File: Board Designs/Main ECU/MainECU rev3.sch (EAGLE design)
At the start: 155 parts, among them Q1 MMBT3904LT3G, Q11 MMBT3904LT3G, Q2 MMBT3904LT3G, Q3 MMBT3904LT3G, Q4 MMBT3904LT3G, Q5 MMBT3904LT3G, Q6 MMBT3904LT3G, Q7 MMBT3904LT3G, Q8 MMBT3904LT3G, Q9 MMBT3904LT3G, X1 CONNECTOR-37, X2 CONNECTOR-4AUTOSPORT, X3 CONNECTOR-4NANO-FIT-VERTICAL-4, X4 CONNECTOR-4NANO-FIT-VERTICAL-4

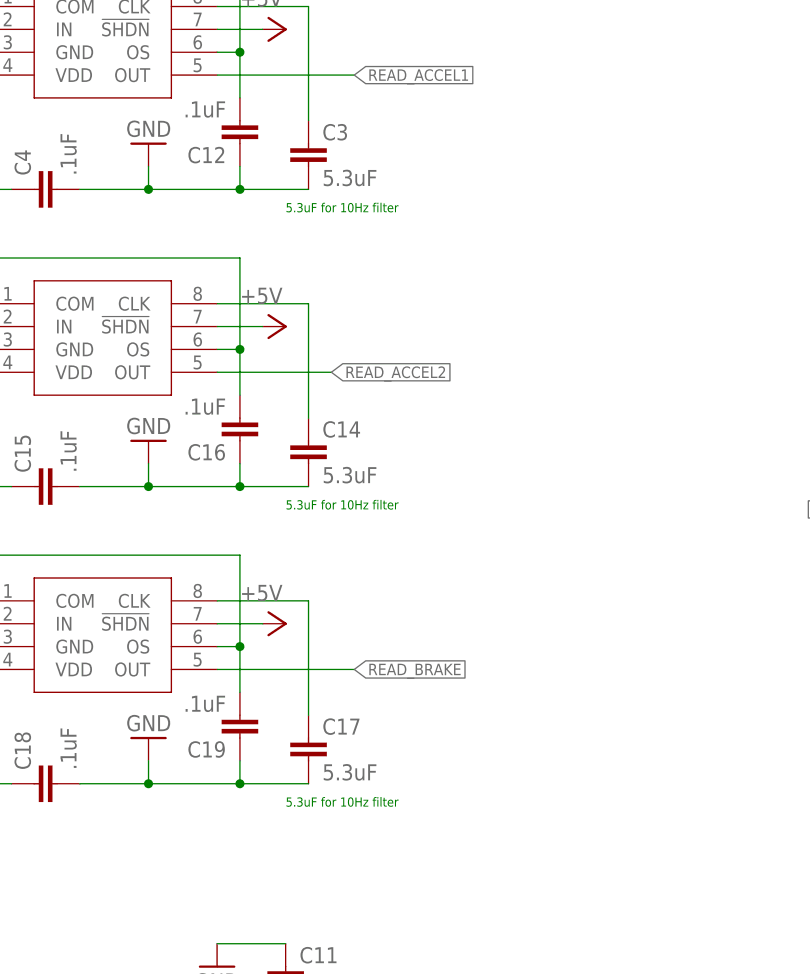
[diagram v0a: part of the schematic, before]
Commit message: Main ECU: [rev2, rev3] Fix filter frequency capacitor values, [rev1b, rev3] shorten a few traces
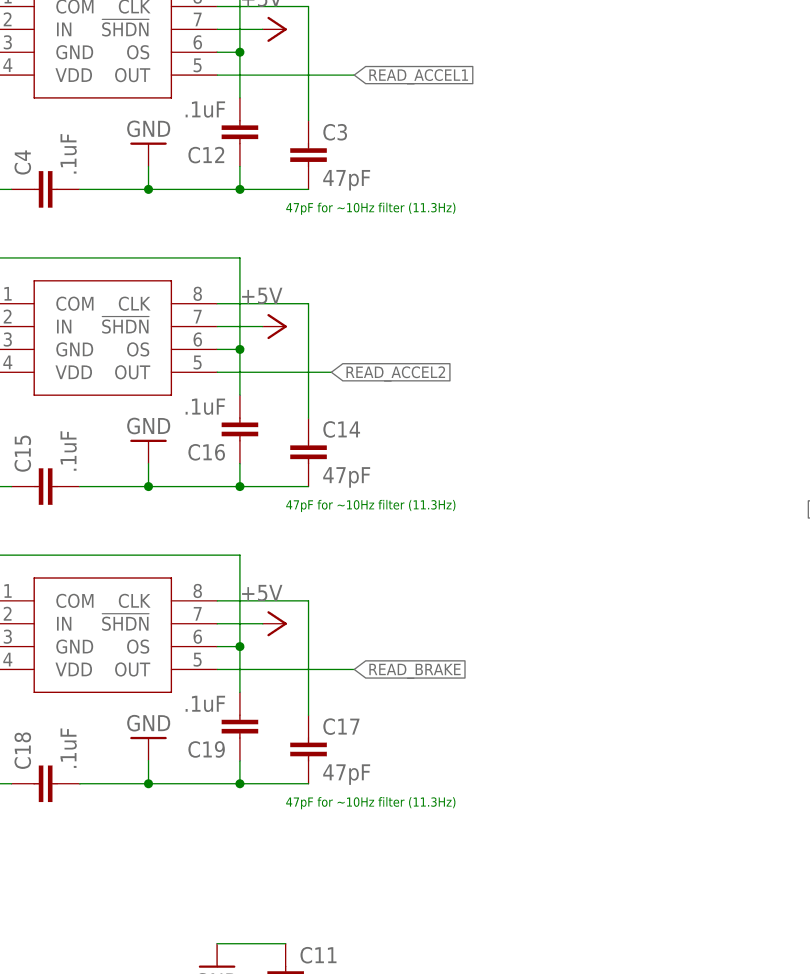
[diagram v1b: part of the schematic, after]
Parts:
- C14, C17, C3: value 5.3uF -> 47pF
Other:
- note added: "47pF for ~10Hz filter (11.3Hz)"
- note removed: "5.3uF for 10Hz filter"
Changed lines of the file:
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@@
 <part name="GND34" library="HyTechSymbols" deviceset="GND" device=""/>
 <part name="U$27" library="HyTechDevices" deviceset="MAX7480" device=""/>
-<part name="C3" library="HyTechDevices" deviceset="CAP" device="0805" value="5.3uF"/>
+<part name="C3" library="HyTechDevices" deviceset="CAP" device="0805" value="47pF"/>
 <part name="C4" library="HyTechDevices" deviceset="CAP" device="0805" value=".1uF"/>
 <part name="C12" library="HyTechDevices" deviceset="CAP" device="0805" value=".1uF"/>
@@
 <part name="P+15" library="supply1" library_urn="urn:adsk.eagle:library:371" deviceset="+5V" device=""/>
 <part name="U$28" library="HyTechDevices" deviceset="MAX7480" device=""/>
-<part name="C14" library="HyTechDevices" deviceset="CAP" device="0805" value="5.3uF"/>
+<part name="C14" library="HyTechDevices" deviceset="CAP" device="0805" value="47pF"/>
 <part name="C15" library="HyTechDevices" deviceset="CAP" device="0805" value=".1uF"/>
 <part name="C16" library="HyTechDevices" deviceset="CAP" device="0805" value=".1uF"/>
@@
 <part name="P+17" library="supply1" library_urn="urn:adsk.eagle:library:371" deviceset="+5V" device=""/>
 <part name="U$26" library="HyTechDevices" deviceset="MAX7480" device=""/>
-<part name="C17" library="HyTechDevices" deviceset="CAP" device="0805" value="5.3uF"/>
+<part name="C17" library="HyTechDevices" deviceset="CAP" device="0805" value="47pF"/>
 <part name="C18" library="HyTechDevices" deviceset="CAP" device="0805" value=".1uF"/>
 <part name="C19" library="HyTechDevices" deviceset="CAP" device="0805" value=".1uF"/>
@@
 <text x="58.42" y="93.98" size="1.016" layer="95">CANL for
 Motor Controller</text>
-<text x="358.14" y="238.76" size="1.016" layer="91">5.3uF for 10Hz filter</text>
-<text x="358.14" y="205.74" size="1.016" layer="91">5.3uF for 10Hz filter</text>
-<text x="358.14" y="172.72" size="1.016" layer="91">5.3uF for 10Hz filter</text>
+<text x="358.14" y="238.76" size="1.016" layer="91">47pF for ~10Hz filter (11.3Hz)</text>
+<text x="358.14" y="205.74" size="1.016" layer="91">47pF for ~10Hz filter (11.3Hz)</text>
+<text x="358.14" y="172.72" size="1.016" layer="91">47pF for ~10Hz filter (11.3Hz)</text>
 <text x="58.42" y="76.2" size="1.27" layer="96">12V for Dash</text>
 <text x="127" y="149.86" size="1.27" layer="96">Check Values, Switching V is 5V</text>

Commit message: Rename Main ECU rev1b -> rev3, rev3 -> rev4
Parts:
- removed C14, C17: 47pF, HyTechDevices:CAP0805
- removed C15, C16, C18, C19, C21: .1uF, HyTechDevices:CAP0805
- removed C20: .22uF, HyTechDevices:CAP0805
- removed CAN_TRANSCEIVER2: MCP2551, HyTechDevices:MCP2551
- removed Q1, Q11, Q2, Q3, Q4, Q5, Q6, Q7, Q8, Q9: MMBT3904LT3G, HyTechDevices:BJT_NPNSOT
- removed Q10: (no value), HyTechDevices:BJT_NPNSOT
- removed R46: 120, HyTechDevices:RESISTOR0805-RES
- removed R47, R50: 2.2k, HyTechDevices:RESISTOR0805-RES
- removed R48: 10k, HyTechDevices:RESISTOR0805-RES
- removed R49: 1.2k, HyTechDevices:RESISTOR0805-RES
- removed REG3: 5V, HyTechDevices:OKI-78SR
- removed U$27, U$28: (no value), HyTechDevices:MAX7480
- added AC1_FILTR, AC2_FILTR: 510, HyTechDevices:RESISTOR0805-RES
- added BRAKE_LIGHT_SSR, FAN_SSR1, FAN_SSR2, INVERTER_SSR, PUMP_SSR: CPC1002N, HyTechDevices:CPC1002N
- added BR_FILTR: 100, HyTechDevices:RESISTOR0805-RES
- added C13: .1uF, HyTechDevices:CAP0805
- added LED12, LED13, LED16, LED4: Red, HyTechDevices:LED-0805
- added R25: 330, HyTechDevices:RESISTOR0805-RES
- added REG2: 5V, HyTechDevices:OKI-78SR
- added U$20, U$21, U$22: JUMPER, HyTechDevices:JUMPER
- C11: value (none) -> .22uF
- C12: value .1uF -> 2.2µ
- C3: value 47pF -> 22µ
- C4: value .1uF -> 22µ
- D7, D8, D9: value MMBZ5246BLT1G -> DIODE0805; device HyTechDevices:DIODE_ZENER -> HyTechDevices:DIODE0805
- R10: value 2.2k -> 43
- R16: value 100 -> 43
- R24, R27, R28: value 10k -> 33
- R35, R36, R38, R39, R40, R41, R42: value 2.2k -> 270
- R37: value 0 -> 270
- R44: value 2.2k -> 0
- U$11, U$12: value JUMPER -> TLP291-4; device HyTechDevices:JUMPER -> HyTechDevices:TLP291-4
- U$15: value BJT_PNPSOT -> SN74LV1T34; device HyTechDevices:BJT_PNPSOT -> HyTechDevices:SN74LV1T34
- U$16: value CR-2450/G1AN -> JUMPER; device HyTechDevices:CR-2450/G1AN -> HyTechDevices:JUMPER
- U$19: value MC34152 -> JUMPER; device HyTechDevices:MC34152 -> HyTechDevices:JUMPER
- U$26: value (none) -> CR-2450/G1AN; device HyTechDevices:MAX7480 -> HyTechDevices:CR-2450/G1AN
- U$4, U$6, U$7: value N-CHANNEL_MOSFET_FQP30N06L -> G5LE; device HyTechDevices:N-CHANNEL_MOSFET_HOR_HOLE -> HyTechDevices:G5LE
- U$5: value MC34152 -> CPC1002N; device HyTechDevices:MC34152 -> HyTechDevices:CPC1002N
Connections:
- removed net DASH_CTRL5_IN: U$12.P$2, U$17.GPA4
- removed net DASH_CTRL5_OUT: R40.1, U$17.GPB4
- removed net DASH_CTRL6_IN: U$11.P$2, U$17.GPA5
- removed net DASH_CTRL6_OUT: R41.1, U$17.GPB5
- removed net DASH_CTRL7_IN: U$13.P$2, U$17.GPA6
- removed net DASH_CTRL7_OUT: R42.1, U$17.GPB6
- removed net DASH_CTRL8_IN: U$14.P$2, U$17.GPA7
- removed net DASH_CTRL8_OUT: R44.1, U$17.GPB7
- removed net FAN1CONTROL: U$1.A8, U$5.IN_A
- removed net FAN1DRIVE: D8.C, R24.2, U$5.OUT_A, U$7.G
- removed net FAN2CONTROL: U$1.A9, U$5.IN_B
- removed net FAN2DRIVE: D7.C, R28.2, U$4.G, U$5.OUT_B
- removed net N$66: D4.A, Q9.COLLECTOR, U$8.COIL-
- removed net PUMPCONTROL: U$1.A6, U$19.IN_A
- removed net PUMPDRIVE: D9.C, R27.2, U$19.OUT_A, U$6.G
- removed net TELEMETRY_CANH: CAN_TRANSCEIVER2.7, R46.2, X4-4.S
- removed net TELEMETRY_CANL: CAN_TRANSCEIVER2.6, R46.1, X4-3.S
- new net DASH_CTRL5: R39.1, U$17.GPA4
- new net DASH_CTRL6: R40.1, U$13.P$2, U$17.GPA5
- new net DASH_CTRL7: R41.1, U$14.P$2, U$17.GPA6
- new net DASH_CTRL8: R42.1, U$15.2, U$17.GPA7, U$19.P$2
- new net N$20: D8.C, FAN_SSR1.DC-, U$7.COIL-
- new net N$39: FAN_SSR2.CONTROL-, LED16.A
- new net N$43: D10.C, R26.1, SOFTWARE_SHUTOFF.COIL-, U$5.DC-
- new net N$44: R25.2, U$5.CONTROL-
- new net RELAY_CTRL1: PUMP_SSR.CONTROL+, U$1.A9
- new net RELAY_CTRL2: FAN_SSR1.CONTROL+, U$1.D2
- new net RELAY_CTRL3: FAN_SSR2.CONTROL+, U$1.A8
- net +12V: now also BRAKE_LIGHT_SSR.DC+, C11.2, FAN_SSR1.DC+, FAN_SSR2.DC+, INVERTER_SSR.DC+, PUMP_SSR.DC+, REG2.IN, U$11.C3, U$11.C4, U$12.C1, U$12.C2, U$12.C3, U$12.C4, U$16.P$1, U$21.P$1, U$5.DC+; no longer C20.2, D10.C, D4.C, R48.1, REG3.IN, SOFTWARE_SHUTOFF.COIL-, U$15.E, U$19.VCC, U$5.VCC, U$8.COIL+
- net +5V: now also U$15.5, U$20.P$1, U$22.P$1; no longer C11.2, C15.1, C18.1, C4.1, U$26.!SHDN, U$26.VDD, U$27.!SHDN, U$27.VDD, U$28.!SHDN, U$28.VDD
- net BRAKE_LIGHT: now also BRAKE_LIGHT_SSR.DC-; no longer U$15.C
- net CANH: now also X4-4.S
- net CANL: now also X4-3.S
- net DASH_CTRL1: now also U$17.GPA0; no longer U$17.GPB0
- net DASH_CTRL10: now also U$17.GPB1; no longer U$17.GPA1
- net DASH_CTRL11: now also U$17.GPB2; no longer U$17.GPA2
- net DASH_CTRL12: now also U$17.GPB3; no longer U$17.GPA3
- net DASH_CTRL2: now also U$17.GPA1; no longer U$17.GPB1
- net DASH_CTRL3: now also R37.1, U$17.GPA2; no longer R38.1, U$17.GPB2
- net DASH_CTRL4: now also R38.1, U$17.GPA3; no longer R39.1, U$17.GPB3
- net DASH_CTRL9: now also U$17.GPB0; no longer U$17.GPA0
- net DASH_IO2: now also R44.2; no longer R37.2
- net DASH_IO3: now also U$12.EM2; no longer Q3.COLLECTOR
- net DASH_IO4: now also U$12.EM1; no longer Q4.COLLECTOR
- net DASH_IO5: now also U$11.EM4; no longer Q5.COLLECTOR, U$12.P$1
- net DASH_IO6: now also U$11.EM3, U$13.P$1; no longer Q6.COLLECTOR, U$11.P$1
- net DASH_IO7: now also U$11.EM2, U$14.P$1; no longer Q7.COLLECTOR, U$13.P$1
- net DASH_IO8: now also U$11.EM1, U$15.4, U$19.P$1; no longer Q8.COLLECTOR, U$14.P$1
- net FAN1-: now also U$7.P; no longer U$7.D
- net FAN2-: now also U$4.P; no longer U$4.D
- net GND: now also C13.1, D10.A, D4.A, LED4.C, R24.2, R25.1, R27.2, R28.2, REG2.GND, SOFTWARE_SHUTOFF.COIL+, U$11.GND1, U$11.GND2, U$11.GND3, U$11.GND4, U$12.GND1, U$12.GND2, U$12.GND3, U$12.GND4, U$15.3, U$4.COIL+, U$6.COIL+, U$7.COIL+, U$8.COIL-; no longer C14.2, C15.2, C16.1, C17.2, C18.2, C19.1, C20.1, C21.1, CAN_TRANSCEIVER2.2, CAN_TRANSCEIVER2.8, Q1.EMITTER, Q10.EMITTER, Q11.EMITTER, Q2.EMITTER, Q3.EMITTER, Q4.EMITTER, Q5.EMITTER, Q6.EMITTER, Q7.EMITTER, Q8.EMITTER, Q9.EMITTER, R24.1, R27.1, R28.1, REG3.GND, U$19.GND, U$25.GND, U$26.GND, U$27.GND, U$28.GND, U$5.GND
- net INVERTER_CTRL: now also INVERTER_SSR.CONTROL+; no longer R16.1, R47.1
- net N$17: now also BRAKE_LIGHT_SSR.CONTROL+, R10.1; no longer Q10.COLLECTOR, R48.2, R49.1
- net N$21: now also D9.C, FAN_SSR2.DC-, U$4.COIL-; no longer C3.1, U$27.CLK
- net N$23: now also AC2_FILTR.1; no longer U$28.IN
- net N$24: now also AC1_FILTR.1; no longer U$27.IN
- net N$25: now also BR_FILTR.1; no longer U$26.IN
- net N$26: now also D4.C, INVERTER_SSR.DC-, U$8.COIL+; no longer Q11.BASE, R50.2
- net N$27: now also INVERTER_SSR.CONTROL-, R16.1; no longer D10.A, Q11.COLLECTOR, SOFTWARE_SHUTOFF.COIL+
- net N$30: now also LED16.C, R24.1; no longer Q2.BASE, R36.2
- net N$36: now also LED13.C, R28.1; no longer C16.2, U$28.COM, U$28.OS
- net N$37: now also LED12.C, R27.1; no longer C19.2, U$26.COM, U$26.OS
- net N$38: now also LED12.A, PUMP_SSR.CONTROL-; no longer C14.1, U$28.CLK
- net N$4: now also D7.C, PUMP_SSR.DC-, U$6.COIL-; no longer C12.2, U$27.COM, U$27.OS
- net N$41: now also U$2.3.3V_2, U$26.+; no longer C17.1, U$26.CLK
- net N$42: now also FAN_SSR1.CONTROL-, LED13.A; no longer Q2.COLLECTOR, R37.1
- net N$51: now also U$12.VCC4; no longer Q1.BASE
- net N$52: now also R36.2, U$12.VCC3; no longer Q3.BASE, R38.2
- net N$53: now also R37.2, U$12.VCC2; no longer Q4.BASE, R39.2
- net N$54: now also R38.2, U$12.VCC1; no longer Q5.BASE, R40.2
- net N$55: now also R39.2, U$11.VCC4; no longer Q6.BASE, R41.2
- net N$56: now also R40.2, U$11.VCC3; no longer Q7.BASE, R42.2
- net N$57: now also R41.2, U$11.VCC2; no longer Q8.BASE, R44.2
- net N$58: now also R42.2, U$11.VCC1; no longer R49.2, U$15.B
- net N$59: now also U$12.EM4; no longer Q1.COLLECTOR
- net N$60: now also R44.1, U$12.EM3; no longer U$16.+, U$2.3.3V_2
- net N$61: now also U$11.C1, U$16.P$2, U$20.P$2; no longer U$16.-, U$2.GND_2
- net N$62: now also U$11.C2, U$21.P$2, U$22.P$2; no longer CAN_TRANSCEIVER2.4, U$2.A15
- net N$64: now also U$2.GND_2, U$26.-; no longer CAN_TRANSCEIVER2.1, U$2.A14
- net N$65: now also U$25.GND; no longer Q9.BASE, R47.2
- net N$7: now also BRAKE_LIGHT_SSR.CONTROL-, LED4.A; no longer Q10.BASE, R10.1
- net PUMP1-: now also U$6.P; no longer U$6.D
- net READ_ACCEL1: now also AC1_FILTR.2, C4.1; no longer U$27.OUT
- net READ_ACCEL2: now also AC2_FILTR.2, C3.1; no longer U$28.OUT
- net READ_BRAKE: now also BR_FILTR.2, C12.2; no longer U$26.OUT
- net SOFTWARE_SHUTDOWN: now also U$5.CONTROL+; no longer R26.1, R50.1
- net TELEMETRY5V: now also C13.2, REG2.OUT; no longer C21.2, CAN_TRANSCEIVER2.3, REG3.OUT
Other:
- note added: "Relays"
- note added: "Use these jumpers or SN74LV1T34 only when optocoupler resistors are removed!"
- note added: "Use these jumpers to select DASH_IO{7,8} output voltage"
- note added: "⇩ Pullup/down resistors to detect open circuit. Install only one per signal on ACCEL1 and ACCEL2."
- note removed: "47pF for ~10Hz filter (11.3Hz)"
- note removed: "Check Values, Switching V is 5V"
- note removed: "Dash 5, 6, 7, 8 Can be inputs or outputs For input, solder jumper. For output, solder transistor and resistor."
- note removed: "Pullup/down resistors to detect open circuit. Install only one per signal on ACCEL1 and ACCEL2."
- moved on the sheet: 5ABOARDFUSE, 5AFUSE, 5ASHUTDOWNFUSE, ACC1_PD, ACC1_PU, ACC2_PD, ACC2_PU, ADXL345_BREAKOUT, BMS_LATCH_SSR, BMS_SSR, BOARD_TEMP, C1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

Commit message: Library: Update XBee footprint, Add zener diode, toggle TXB010{4,6} value option; MainECU rev1b: add SPI level shifter, switch to separate SPI CS pins, move RTC batt inside board footprint; MainECU rev3: init
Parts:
- removed AC1_FILTR, AC2_FILTR: 510, HyTechDevices:RESISTOR0805-RES
- removed BRAKE_LIGHT_SSR, FAN_SSR1, FAN_SSR2, PUMP_SSR: CPC1002N, HyTechDevices:CPC1002N
- removed BR_FILTR: 100, HyTechDevices:RESISTOR0805-RES
- removed C13: .1uF, HyTechDevices:CAP0805
- removed D7, D8, D9: DIODE0805, HyTechDevices:DIODE0805
- removed LED12, LED13, LED16, LED4: Red, HyTechDevices:LED-0805
- removed REG2: 5V, HyTechDevices:OKI-78SR
- removed U$19, U$20, U$21, U$22: JUMPER, HyTechDevices:JUMPER
- removed U$25: TXB0104TSSOP, HyTechDevices:TXB0104TSSOP
- added C14, C17: 5.3uF, HyTechDevices:CAP0805
- added C15, C16, C18, C19, C21: .1uF, HyTechDevices:CAP0805
- added C20: .22uF, HyTechDevices:CAP0805
- added CAN_TRANSCEIVER2: MCP2551, HyTechDevices:MCP2551
- added Q1, Q10, Q2, Q3, Q4, Q5, Q6, Q7, Q8: (no value), HyTechDevices:BJT_NPNSOT
- added R46: 120, HyTechDevices:RESISTOR0805-RES
- added R48: 10k, HyTechDevices:RESISTOR0805-RES
- added R49: 1.2k, HyTechDevices:RESISTOR0805-RES
- added REG3: 5V, HyTechDevices:OKI-78SR
- added U$27, U$28: (no value), HyTechDevices:MAX7480
- C11: value .22uF -> (none)
- C12: value 2.2µ -> .1uF
- C3: value 22µ -> 5.3uF
- C4: value 22µ -> .1uF
- R10: value 43 -> 2.2k
- R24, R27, R28: value 33 -> 10k
- R35, R36, R38, R39, R40, R41, R42: value 270 -> 2.2k
- R37: value 270 -> 0
- R44: value 0 -> 2.2k
- U$11, U$12: value TLP291-4 -> JUMPER; device HyTechDevices:TLP291-4 -> HyTechDevices:JUMPER
- U$15: value SN74LV1T34 -> BJT_PNPSOT; device HyTechDevices:SN74LV1T34 -> HyTechDevices:BJT_PNPSOT
- U$16: value JUMPER -> CR-2450/G1AN; device HyTechDevices:JUMPER -> HyTechDevices:CR-2450/G1AN
- U$26: value CR-2450/G1AN -> (none); device HyTechDevices:CR-2450/G1AN -> HyTechDevices:MAX7480
- U$4, U$6, U$7: value G5LE -> N-CHANNEL_MOSFET_HOR_HOLE; device HyTechDevices:G5LE -> HyTechDevices:N-CHANNEL_MOSFET_HOR_HOLE
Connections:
- removed net 3.3V_MAIN_TEENSY: U$1.3.3V, U$25.VCCA
- removed net CS1_5V: U$18.!CS!/SHDN, U$25.B1
- removed net CS1_TEENSY: U$1.D9(RX2), U$25.A1
- removed net CS2_5V: U$17.!CS, U$25.B2
- removed net CS2_TEENSY: U$1.D10(TX2), U$25.A2
- removed net DASH_CTRL5: R39.1, U$17.GPA4
- removed net DASH_CTRL6: R40.1, U$13.P$2, U$17.GPA5
- removed net DASH_CTRL7: R41.1, U$14.P$2, U$17.GPA6
- removed net DASH_CTRL8: R42.1, U$15.2, U$17.GPA7, U$19.P$2
- removed net MOSI_5V: U$17.SI, U$18.DIN, U$25.B4
- removed net N$20: D8.C, FAN_SSR1.DC-, U$7.COIL-
- removed net N$39: FAN_SSR2.CONTROL-, LED16.A
- removed net N$65: U$25.GND
- removed net RELAY_CTRL1: PUMP_SSR.CONTROL+, U$1.A9
- removed net RELAY_CTRL2: FAN_SSR1.CONTROL+, U$1.D2
- removed net RELAY_CTRL3: FAN_SSR2.CONTROL+, U$1.A8
- removed net SCK_5V: U$17.SCK, U$18.CLK, U$25.B3
- new net CHIP_SELECT1: U$1.D9(RX2), U$18.!CS!/SHDN
- new net CHIP_SELECT2: U$1.D10(TX2), U$17.!CS
- new net DASH_CTRL5_IN: U$12.P$2, U$17.GPA4
- new net DASH_CTRL5_OUT: R40.1, U$17.GPB4
- new net DASH_CTRL6_IN: U$11.P$2, U$17.GPA5
- new net DASH_CTRL6_OUT: R41.1, U$17.GPB5
- new net DASH_CTRL7_IN: U$13.P$2, U$17.GPA6
- new net DASH_CTRL7_OUT: R42.1, U$17.GPB6
- new net DASH_CTRL8_IN: U$14.P$2, U$17.GPA7
- new net DASH_CTRL8_OUT: R44.1, U$17.GPB7
- new net FAN1CONTROL: R24.2, U$1.A8, U$7.G
- new net FAN2CONTROL: R28.2, U$1.A9, U$4.G
- new net PUMPCONTROL: R27.2, U$1.A6, U$6.G
- new net TELEMETRY_CANH: CAN_TRANSCEIVER2.7, R46.2, X4-4.S
- new net TELEMETRY_CANL: CAN_TRANSCEIVER2.6, R46.1, X4-3.S
- net +12V: now also C20.2, R48.1, REG3.IN, U$15.E; no longer BRAKE_LIGHT_SSR.DC+, C11.2, FAN_SSR1.DC+, FAN_SSR2.DC+, PUMP_SSR.DC+, REG2.IN, U$11.C3, U$11.C4, U$12.C1, U$12.C2, U$12.C3, U$12.C4, U$16.P$1, U$21.P$1
- net +5V: now also C11.2, C15.1, C18.1, C4.1, U$26.!SHDN, U$26.VDD, U$27.!SHDN, U$27.VDD, U$28.!SHDN, U$28.VDD; no longer U$15.5, U$20.P$1, U$22.P$1, U$25.VCCB
- net BRAKE_LIGHT: now also U$15.C; no longer BRAKE_LIGHT_SSR.DC-
- net CANH: no longer X4-4.S
- net CANL: no longer X4-3.S
- net DASH_CTRL1: now also U$17.GPB0; no longer U$17.GPA0
- net DASH_CTRL10: now also U$17.GPA1; no longer U$17.GPB1
- net DASH_CTRL11: now also U$17.GPA2; no longer U$17.GPB2
- net DASH_CTRL12: now also U$17.GPA3; no longer U$17.GPB3
- net DASH_CTRL2: now also U$17.GPB1; no longer U$17.GPA1
- net DASH_CTRL3: now also R38.1, U$17.GPB2; no longer R37.1, U$17.GPA2
- net DASH_CTRL4: now also R39.1, U$17.GPB3; no longer R38.1, U$17.GPA3
- net DASH_CTRL9: now also U$17.GPA0; no longer U$17.GPB0
- net DASH_IO2: now also R37.2; no longer R44.2
- net DASH_IO3: now also Q3.COLLECTOR; no longer U$12.EM2
- net DASH_IO4: now also Q4.COLLECTOR; no longer U$12.EM1
- net DASH_IO5: now also Q5.COLLECTOR, U$12.P$1; no longer U$11.EM4
- net DASH_IO6: now also Q6.COLLECTOR, U$11.P$1; no longer U$11.EM3, U$13.P$1
- net DASH_IO7: now also Q7.COLLECTOR, U$13.P$1; no longer U$11.EM2, U$14.P$1
- net DASH_IO8: now also Q8.COLLECTOR, U$14.P$1; no longer U$11.EM1, U$15.4, U$19.P$1
- net FAN1-: now also U$7.D; no longer U$7.P
- net FAN2-: now also U$4.D; no longer U$4.P
- net GND: now also C14.2, C15.2, C16.1, C17.2, C18.2, C19.1, C20.1, C21.1, CAN_TRANSCEIVER2.2, CAN_TRANSCEIVER2.8, Q1.EMITTER, Q10.EMITTER, Q2.EMITTER, Q3.EMITTER, Q4.EMITTER, Q5.EMITTER, Q6.EMITTER, Q7.EMITTER, Q8.EMITTER, R24.1, R27.1, R28.1, REG3.GND, U$26.GND, U$27.GND, U$28.GND; no longer C13.1, D7.A, D8.A, D9.A, LED4.C, R24.2, R27.2, R28.2, REG2.GND, U$11.GND1, U$11.GND2, U$11.GND3, U$11.GND4, U$12.GND1, U$12.GND2, U$12.GND3, U$12.GND4, U$15.3, U$25.OE, U$4.COIL+, U$6.COIL+, U$7.COIL+
- net MOSI_TEENSY: now also U$17.SI, U$18.DIN; no longer U$25.A4
- net N$17: now also Q10.COLLECTOR, R48.2, R49.1; no longer BRAKE_LIGHT_SSR.CONTROL+, R10.1
- net N$21: now also C3.1, U$27.CLK; no longer D9.C, FAN_SSR2.DC-, U$4.COIL-
- net N$23: now also U$28.IN; no longer AC2_FILTR.1
- net N$24: now also U$27.IN; no longer AC1_FILTR.1
- net N$25: now also U$26.IN; no longer BR_FILTR.1
- net N$30: now also Q2.BASE, R36.2; no longer LED16.C, R24.1
- net N$36: now also C16.2, U$28.COM, U$28.OS; no longer LED13.C, R28.1
- net N$37: now also C19.2, U$26.COM, U$26.OS; no longer LED12.C, R27.1
- net N$38: now also C14.1, U$28.CLK; no longer LED12.A, PUMP_SSR.CONTROL-
- net N$4: now also C12.2, U$27.COM, U$27.OS; no longer D7.C, PUMP_SSR.DC-, U$6.COIL-
- net N$41: now also C17.1, U$26.CLK; no longer U$2.3.3V_2, U$26.+
- net N$42: now also Q2.COLLECTOR, R37.1; no longer FAN_SSR1.CONTROL-, LED13.A
- net N$51: now also Q1.BASE; no longer U$12.VCC4
- net N$52: now also Q3.BASE, R38.2; no longer R36.2, U$12.VCC3
- net N$53: now also Q4.BASE, R39.2; no longer R37.2, U$12.VCC2
- net N$54: now also Q5.BASE, R40.2; no longer R38.2, U$12.VCC1
- net N$55: now also Q6.BASE, R41.2; no longer R39.2, U$11.VCC4
- net N$56: now also Q7.BASE, R42.2; no longer R40.2, U$11.VCC3
- net N$57: now also Q8.BASE, R44.2; no longer R41.2, U$11.VCC2
- net N$58: now also R49.2, U$15.B; no longer R42.2, U$11.VCC1
- net N$59: now also Q1.COLLECTOR; no longer U$12.EM4
- net N$60: now also U$16.+, U$2.3.3V_2; no longer R44.1, U$12.EM3
- net N$61: now also U$16.-, U$2.GND_2; no longer U$11.C1, U$16.P$2, U$20.P$2
- net N$62: now also CAN_TRANSCEIVER2.4, U$2.A15; no longer U$11.C2, U$21.P$2, U$22.P$2
- net N$64: now also CAN_TRANSCEIVER2.1, U$2.A14; no longer U$2.GND_2, U$26.-
- net N$7: now also Q10.BASE, R10.1; no longer BRAKE_LIGHT_SSR.CONTROL-, LED4.A
- net PUMP1-: now also U$6.D; no longer U$6.P
- net READ_ACCEL1: now also U$27.OUT; no longer AC1_FILTR.2, C4.1
- net READ_ACCEL2: now also U$28.OUT; no longer AC2_FILTR.2, C3.1
- net READ_BRAKE: now also U$26.OUT; no longer BR_FILTR.2, C12.2
- net SCK_TEENSY: now also U$17.SCK, U$18.CLK; no longer U$25.A3
- net TELEMETRY5V: now also C21.2, CAN_TRANSCEIVER2.3, REG3.OUT; no longer C13.2, REG2.OUT
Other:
- note added: "5.3uF for 10Hz filter"
- note added: "Check Values, Switching V is 5V"
- note added: "Dash 5, 6, 7, 8 Can be inputs or outputs For input, solder jumper. For output, solder transistor and resistor."
- note added: "⇦ Pullup/down resistors to detect open circuit. Install only one per signal on ACCEL1 and ACCEL2."
- note removed: "Relays"
- note removed: "Use these jumpers or SN74LV1T34 only when optocoupler resistors are removed!"
- note removed: "Use these jumpers to select DASH_IO{7,8} output voltage"
- note removed: "⇩ Pullup/down resistors to detect open circuit. Install only one per signal on ACCEL1 and ACCEL2."
- moved on the sheet: 5ABOARDFUSE, 5AFUSE, 5ASHUTDOWNFUSE, ACC1_PD, ACC1_PU, ACC2_PD, ACC2_PU, ADXL345_BREAKOUT, BMS_LATCH_SSR, BMS_SSR, BOARD_TEMP, C1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

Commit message: MainECU rev3: Move RTC battery to within board footprint, update XBee package size, add SPI level shifter, Add mosfet drivers and zener diodes, Replace relay control SSRs with transistors
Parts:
- removed INVERTER_SSR: CPC1002N, HyTechDevices:CPC1002N
- removed R25: 330, HyTechDevices:RESISTOR0805-RES
- added D7, D8, D9: MMBZ5246BLT1G, HyTechDevices:DIODE_ZENER
- added Q11, Q9: MMBT3904LT3G, HyTechDevices:BJT_NPNSOT
- added R47, R50: 2.2k, HyTechDevices:RESISTOR0805-RES
- added U$19: MC34152, HyTechDevices:MC34152
- added U$25: TXB0104TSSOP, HyTechDevices:TXB0104TSSOP
- Q1, Q2, Q3, Q4, Q5, Q6, Q7, Q8: value (none) -> MMBT3904LT3G
- R16: value 43 -> 100
- U$4, U$6, U$7: value N-CHANNEL_MOSFET_HOR_HOLE -> N-CHANNEL_MOSFET_FQP30N06L
- U$5: value CPC1002N -> MC34152; device HyTechDevices:CPC1002N -> HyTechDevices:MC34152
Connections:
- removed net CHIP_SELECT1: U$1.D9(RX2), U$18.!CS!/SHDN
- removed net CHIP_SELECT2: U$1.D10(TX2), U$17.!CS
- removed net N$43: D10.C, R26.1, SOFTWARE_SHUTOFF.COIL-, U$5.DC-
- removed net N$44: R25.2, U$5.CONTROL-
- new net 3.3V_MAIN_TEENSY: U$1.3.3V, U$25.VCCA
- new net CS1_5V: U$18.!CS!/SHDN, U$25.B1
- new net CS1_TEENSY: U$1.D9(RX2), U$25.A1
- new net CS2_5V: U$17.!CS, U$25.B2
- new net CS2_TEENSY: U$1.D10(TX2), U$25.A2
- new net FAN1DRIVE: D8.C, R24.2, U$5.OUT_A, U$7.G
- new net FAN2DRIVE: D7.C, R28.2, U$4.G, U$5.OUT_B
- new net MOSI_5V: U$17.SI, U$18.DIN, U$25.B4
- new net N$65: Q9.BASE, R47.2
- new net N$66: D4.A, Q9.COLLECTOR, U$8.COIL-
- new net PUMPDRIVE: D9.C, R27.2, U$19.OUT_A, U$6.G
- new net SCK_5V: U$17.SCK, U$18.CLK, U$25.B3
- net +12V: now also D10.C, D4.C, SOFTWARE_SHUTOFF.COIL-, U$19.VCC, U$5.VCC, U$8.COIL+; no longer INVERTER_SSR.DC+, U$5.DC+
- net +5V: now also U$25.VCCB
- net FAN1CONTROL: now also U$5.IN_A; no longer R24.2, U$7.G
- net FAN2CONTROL: now also U$5.IN_B; no longer R28.2, U$4.G
- net GND: now also D7.A, D8.A, D9.A, Q11.EMITTER, Q9.EMITTER, U$19.GND, U$25.GND, U$25.OE, U$5.GND; no longer D10.A, D4.A, R25.1, SOFTWARE_SHUTOFF.COIL+, U$8.COIL-
- net INVERTER_CTRL: now also R16.1, R47.1; no longer INVERTER_SSR.CONTROL+
- net MOSI_TEENSY: now also U$25.A4; no longer U$17.SI, U$18.DIN
- net N$26: now also Q11.BASE, R50.2; no longer D4.C, INVERTER_SSR.DC-, U$8.COIL+
- net N$27: now also D10.A, Q11.COLLECTOR, SOFTWARE_SHUTOFF.COIL+; no longer INVERTER_SSR.CONTROL-, R16.1
- net PUMPCONTROL: now also U$19.IN_A; no longer R27.2, U$6.G
- net SCK_TEENSY: now also U$25.A3; no longer U$17.SCK, U$18.CLK
- net SOFTWARE_SHUTDOWN: now also R26.1, R50.1; no longer U$5.CONTROL+
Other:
- note added: "Pullup/down resistors to detect open circuit. Install only one per signal on ACCEL1 and ACCEL2."
- note removed: "⇦ Pullup/down resistors to detect open circuit. Install only one per signal on ACCEL1 and ACCEL2."
- moved on the sheet: ACC1_PD, ACC1_PU, ACC2_PD, ACC2_PU, ADXL345_BREAKOUT, BOARD_TEMP, C10, C11, C12, C14, C15, C16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
